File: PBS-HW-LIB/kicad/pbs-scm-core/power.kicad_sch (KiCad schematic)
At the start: 18 parts, among them J1 Host connector, blind-mate, s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, U1 Input TVS and EMI filter, U10 Current-limited load switch (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, U11 Current-limited load switch (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, U12 Current-limited load switch (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, U2 Hot-swap controller with inru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, U3 Swap-detect conditioning (com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, U4 Hold-up controller (ideal dio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, U5 Wide-input DC-DC buck convert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, U6 Point-of-load regulators (3.3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, U7 Voltage supervisor with watch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, U8 Current-limited load switch (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, U9 Current-limited load switch (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

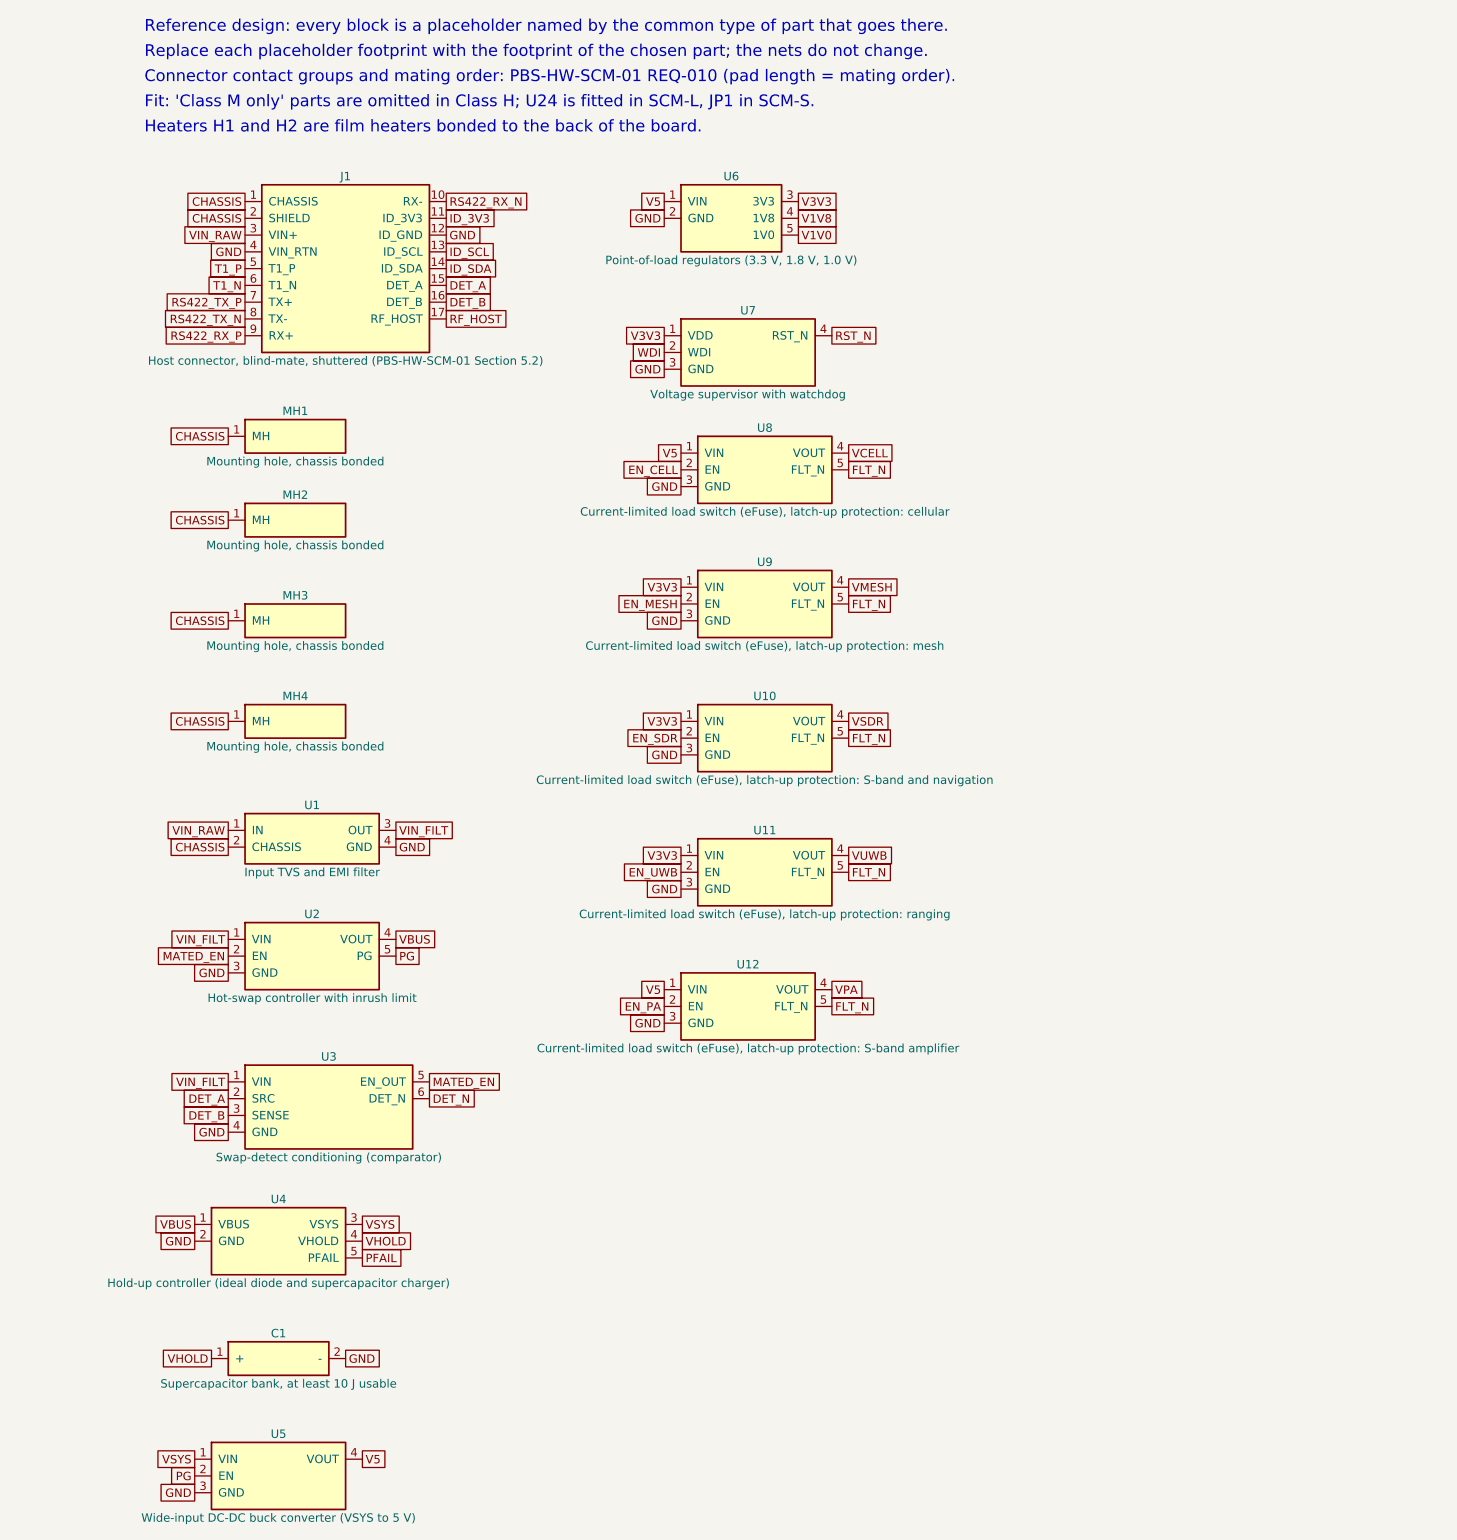
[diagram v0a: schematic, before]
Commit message: Define the module host connector (PBS-HW-CON-01)
Add PBS-HW-CON-01: a face-to-face blind-mate connector with 17 contacts at
stated positions, flat pads on the module and spring contacts in the bay,
mating order set by four free heights 0.60 mm apart, keyed guide pins
(A 4.00, B 3.00), a bay cover plate and covered module apertures, an SMP
RF contact, forces and electrical ratings. Two dimensioned drawing sheets.

KiCad: both J1 footprints now follow the contact map (module half on the
back of the core board, centred; bay half with spring-contact holes and
guide pins), with 3D models showing contact heights, guide pins and the
cover plate. All geometry comes from tools/connector.py.

PBS-HW-SCM-01 v0.3 references the connector document.
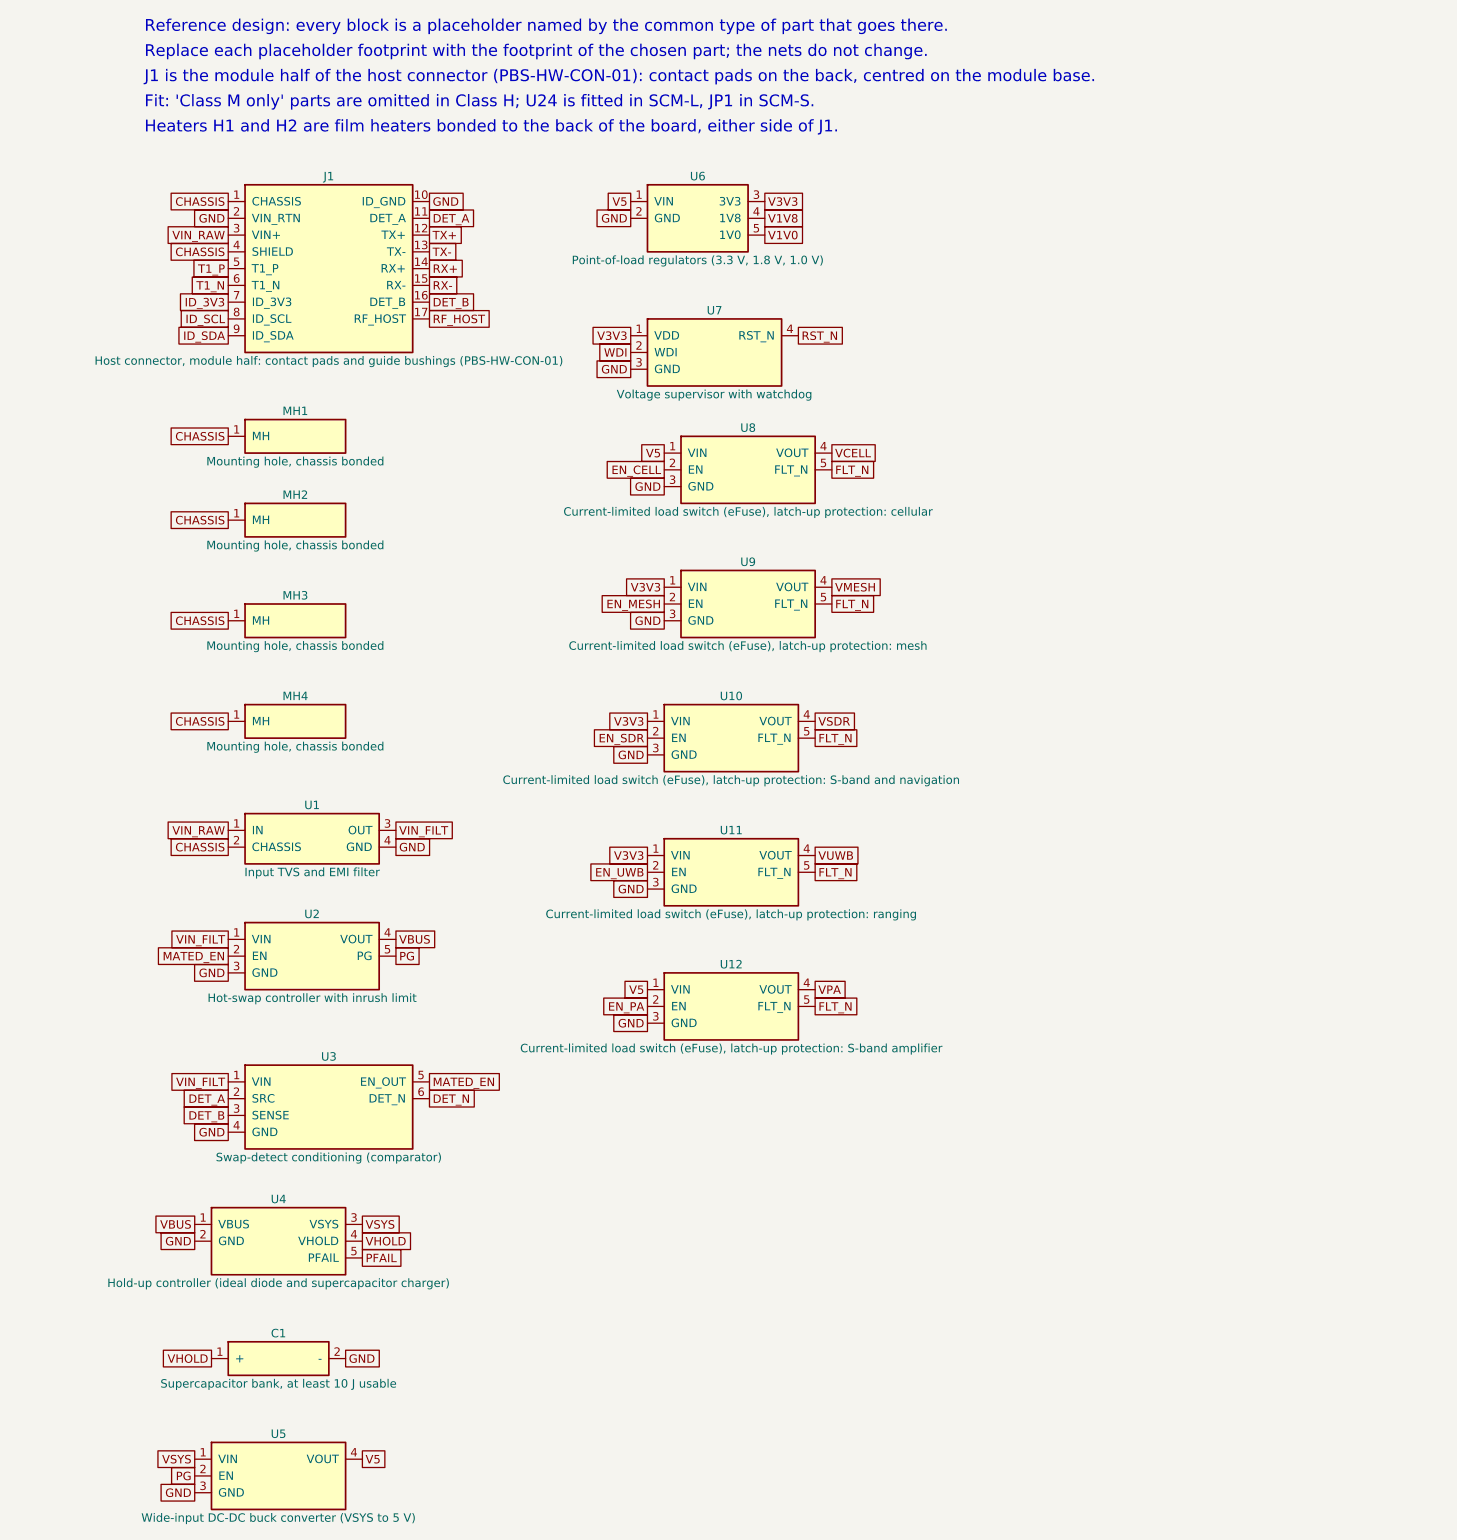
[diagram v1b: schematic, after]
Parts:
- J1: value Host connector, blind-mate, shuttered (PBS-HW-SCM-01 Section 5.2) -> Host connector, module half: contact pads and guide bushings (PBS-HW-CON-01); footprint PBS_Generic:J1_Host_connector_blind_mate_shuttered_PBS_HW_SCM_01_Section_5_2 -> PBS_Generic:J1_Host_connector_module_half_contact_pads_and_guide_bushings_PBS_HW_CON_01; symbol PBS_Generic:J1_Host_connector_blind_mate_shuttered_PBS_HW_SCM_01_Section_5_2 -> PBS_Generic:J1_Host_connector_module_half_contact_pads_and_guide_bushings_PBS_HW_CON_01
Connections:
- net RS422_RX_N is gone; now on net GND: J1.10 (ID_GND)
- net RS422_RX_P is gone; now on net ID_SDA: J1.9 (ID_SDA)
- net RS422_TX_N is gone; now on net ID_SCL: J1.8 (ID_SCL)
- net RS422_TX_P is gone; now on net ID_3V3: J1.7 (ID_3V3)
- net CHASSIS: now also J1.4 (SHIELD); no longer J1.2 (SHIELD)
- net DET_A: now also J1.11 (DET_A); no longer J1.15 (DET_A)
- net GND: now also J1.2 (VIN_RTN); no longer J1.12 (ID_GND), J1.4 (VIN_RTN)
- net ID_3V3: no longer J1.11 (ID_3V3)
- net ID_SCL: no longer J1.13 (ID_SCL)
- net ID_SDA: no longer J1.14 (ID_SDA)
- new net RX+: J1.14 (RX+)
- new net RX-: J1.15 (RX-)
- new net TX+: J1.12 (TX+)
- new net TX-: J1.13 (TX-)
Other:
- note added: "Heaters H1 and H2 are film heaters bonded to the back of the board, either side of J1."
- note added: "J1 is the module half of the host connector (PBS-HW-CON-01): contact pads on the back, centred on the module base."
- note removed: "Connector contact groups and mating order: PBS-HW-SCM-01 REQ-010 (pad length = mating order)."
- note removed: "Heaters H1 and H2 are film heaters bonded to the back of the board."
- moved on the sheet: J1, U10, U11, U12, U6, U7, U8, U9
